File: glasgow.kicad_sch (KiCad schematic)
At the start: 90 parts, among them SW1 RST, U18 TPD3S014, U19 CY7C68013A-56LTX, U20 CAT24M01X, U21 BL24C256A-SFRC, U22 ICE40HX8K-BG121, U23 APX811-40UG-7, U24 TLV75533PDRVR, U25 TLV73312PQDRVR, Y2 24M

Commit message: more fixes, tweaks, pretty
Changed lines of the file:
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@@
 	(wire
 		(pts
-			(xy 217.17 106.68) (xy 217.17 109.22)
+			(xy 217.17 106.68) (xy 217.17 114.3)
 		)
 		(stroke
@@
 	)
 	(label "SWSH"
-		(at 217.17 109.22 270)
-		(effects
-			(font
+		(at 217.17 114.3 270)
+		(effects
+			(font

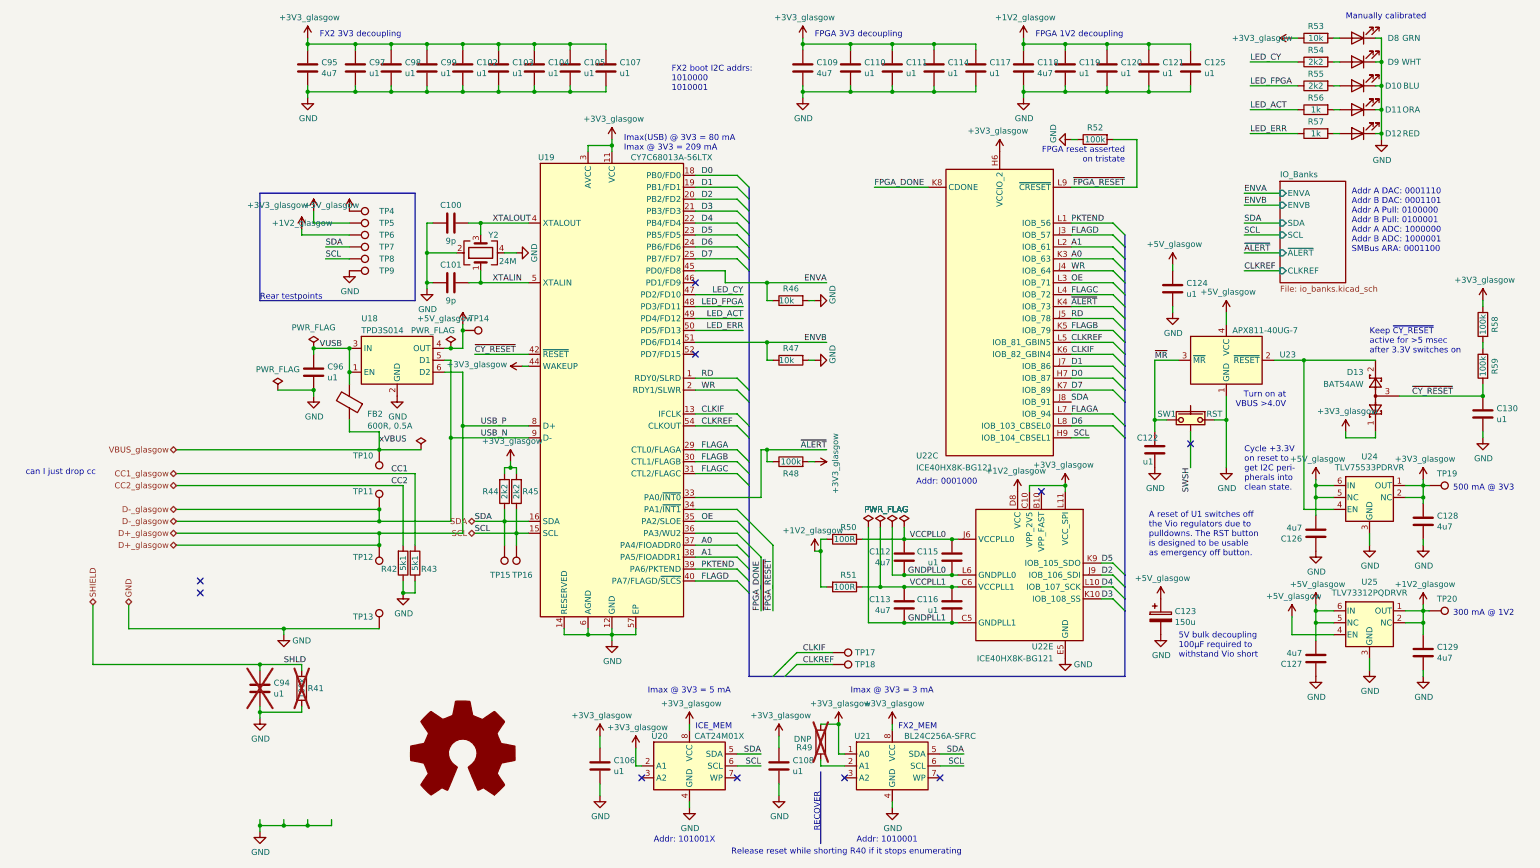
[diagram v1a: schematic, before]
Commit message: added USB-C
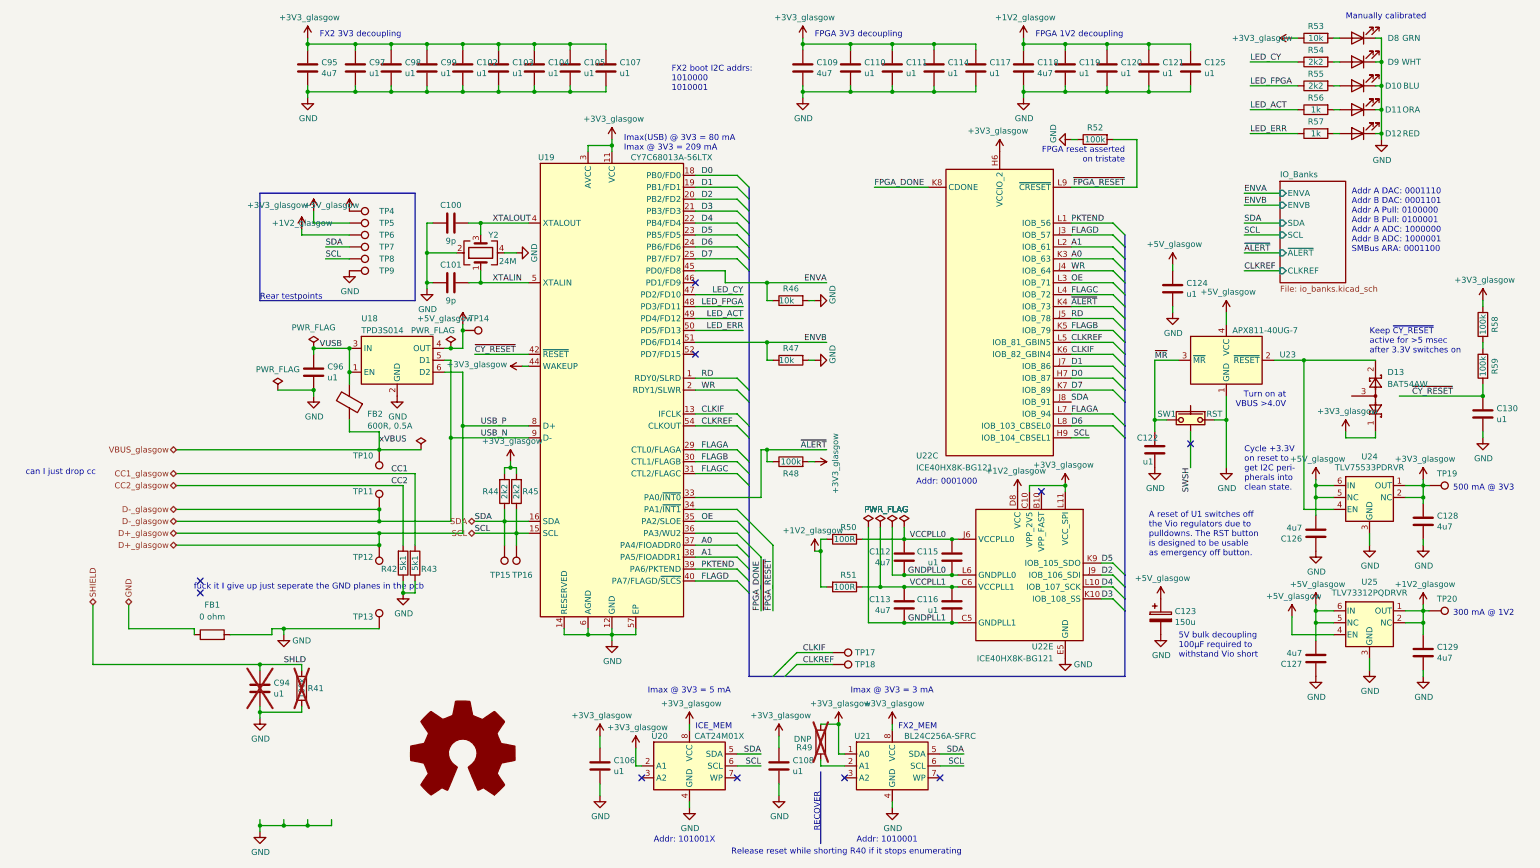
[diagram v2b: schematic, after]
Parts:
- added FB1: 0 ohm, A_HDJ_Library:Fuse_0805_2012Metric, symbol Device:R
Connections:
- net GND: now also FB1.1, FB1.2
- net ~{CY_RESET}: no longer D13.3
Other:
- note added: "fuck it I give up just seperate the GND planes in the pcb"
- moved on the sheet: D13
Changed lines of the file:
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@@
 		)
 	)
+	(text "fuck it I give up just seperate the GND planes in the pcb\n"
+		(exclude_from_sim no)
+		(at 29.464 139.7 0)
+		(effects
+			(font
+				(size 1.27 1.27)
+			)
+		)
+	)
 	(text "FX2_MEM"
 		(exclude_from_sim no)
@@
 	)
 	(junction
+		(at 24.13 148.59)
+		(diameter 0)
+		(color 0 0 0 0)
+	)
+	(junction
 		(at 156.21 129.54)
 		(diameter 0)
@@
 	)
 	(junction
-		(at 24.13 148.59)
-		(diameter 0)
-		(color 0 0 0 0)
-	)
-	(junction
 		(at 46.99 24.13)
 		(diameter 0)
@@
 	(wire
 		(pts
+			(xy 21.59 148.59) (xy 24.13 148.59)
+		)
+		(stroke
+			(width 0)
+			(type default)
+		)
+	)
+	(wire
+		(pts
 			(xy 92.71 34.29) (xy 85.09 34.29)
 		)
@@
 	(wire
 		(pts
+			(xy 24.13 148.59) (xy 44.45 148.59)
+		)
+		(stroke
+			(width 0)
+			(type default)
+		)
+	)
+	(wire
+		(pts
 			(xy 181.61 22.86) (xy 181.61 24.13)
 		)
@@
 		)
 	)
+	(wire
+		(pts
+			(xy 21.59 149.86) (xy 21.59 148.59)
+		)
+		(stroke
+			(width 0)
+			(type default)
+		)
+	)
 	(bus
 		(pts
@@
 	(wire
 		(pts
+			(xy 5.08 148.59) (xy 5.08 149.86)
+		)
+		(stroke
+			(width 0)
+			(type default)
+		)
+	)
+	(wire
+		(pts
 			(xy 59.69 107.95) (xy 76.2 107.95)
 		)
@@
 	(wire
 		(pts
-			(xy 24.13 148.59) (xy 44.45 148.59)
-		)
-		(stroke
-			(width 0)
-			(type default)
-		)
-	)
-	(wire
-		(pts
 			(xy 92.71 24.13) (xy 85.09 24.13)
 		)
@@
 	(wire
 		(pts
+			(xy 255.27 128.27) (xy 255.27 130.81)
+		)
+		(stroke
+			(width 0)
+			(type default)
+		)
+	)
+	(wire
+		(pts
 			(xy 39.37 34.29) (xy 46.99 34.29)
 		)
@@
 	(wire
 		(pts
+			(xy -8.89 148.59) (xy 5.08 148.59)
+		)
+		(stroke
+			(width 0)
+			(type default)
+		)
+	)
+	(wire
+		(pts
 			(xy 191.77 80.01) (xy 200.66 80.01)
 		)
@@
 	(wire
 		(pts
-			(xy -8.89 148.59) (xy 24.13 148.59)
-		)
-		(stroke
-			(width 0)
-			(type default)
-		)
-	)
-	(wire
-		(pts
-			(xy 255.27 128.27) (xy 255.27 130.81)
-		)
-		(stroke
-			(width 0)
-			(type default)
-		)
-	)
-	(wire
-		(pts
 			(xy 1.27 115.57) (xy 52.07 115.57)
 		)
@@
 	(wire
 		(pts
+			(xy 12.7 149.86) (xy 21.59 149.86)
+		)
+		(stroke
+			(width 0)
+			(type default)
+		)
+	)
+	(wire
+		(pts
 			(xy 111.76 52.07) (xy 120.65 52.07)
 		)
@@
 	(symbol
 		(lib_id "Diode:BAT54AW")
-		(at 256.54 99.06 90)
+		(at 256.54 99.06 270)
+		(mirror x)
 		(unit 1)
 		(body_style 1)
@@
 		(dnp no)
 		(property "Reference" "D13"
-			(at 254 93.98 90)
+			(at 259.08 93.98 90)
 			(show_name no)
 			(do_not_autoplace no)
@@
 		)
 		(property "Value" "BAT54AW"
-			(at 254 96.52 90)
+			(at 259.08 96.52 90)
 			(show_name no)
 			(do_not_autoplace no)
@@
 		)
 		(property "Footprint" "Glasgow:SOT-323_SC-70"
-			(at 253.365 97.155 0)
+			(at 259.715 97.155 0)
 			(hide yes)
 			(show_name no)
@@
 					(unit 1)
 				)
+			)
+		)
+	)
+	(symbol
+		(lib_id "Device:R")
+		(at 8.89 149.86 90)
+		(unit 1)
+		(body_style 1)
+		(exclude_from_sim no)
+		(in_bom yes)
+		(on_board yes)
+		(in_pos_files yes)
+		(dnp no)
+		(fields_autoplaced yes)
+		(property "Reference" "FB1"
+			(at 8.89 143.51 90)
+			(show_name no)
+			(do_not_autoplace no)
+			(effects
+				(font
+					(size 1.27 1.27)
+				)
+			)
+		)
+		(property "Value" "0 ohm"
+			(at 8.89 146.05 90)
+			(show_name no)
+			(do_not_autoplace no)
+			(effects
+				(font
+					(size 1.27 1.27)
+				)
+			)
+		)
+		(property "Footprint" "A_HDJ_Library:Fuse_0805_2012Metric"
+			(at 8.89 151.638 90)
+			(hide yes)
+			(show_name no)
+			(do_not_autoplace no)
+			(effects
+				(font
+					(size 1.27 1.27)
+				)
+			)
+		)
+		(property "Datasheet" ""
+			(at 8.89 149.86 0)
+			(hide yes)
+			(show_name no)
+			(do_not_autoplace no)
+			(effects
+				(font
+					(size 1.27 1.27)
+				)
+			)
+		)
+		(property "Description" "Resistor"
+			(at 8.89 149.86 0)
+			(hide yes)
+			(show_name no)
+			(do_not_autoplace no)
+			(effects
+				(font
+					(size 1.27 1.27)
+				)
+			)
+		)
+		(pin "1"
+		)
+		(pin "2"
+		)
+		(instances
+			(project "microcyber"
+				(path "/7ac319af-771c-4997-a005-b73a4a9b44ab/caa76144-87f3-4ce6-9e9c-dcd9e43abe5f"
+					(reference "FB1")
+					(unit 1)
+				)

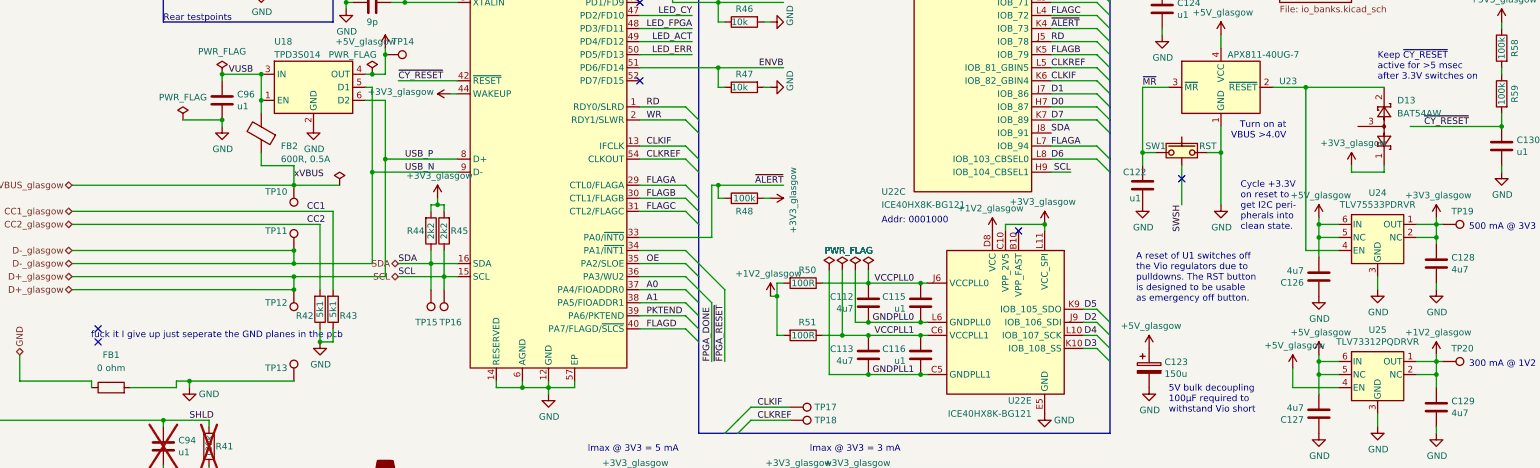
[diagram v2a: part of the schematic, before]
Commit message: added MPN to all parts by hand :'(
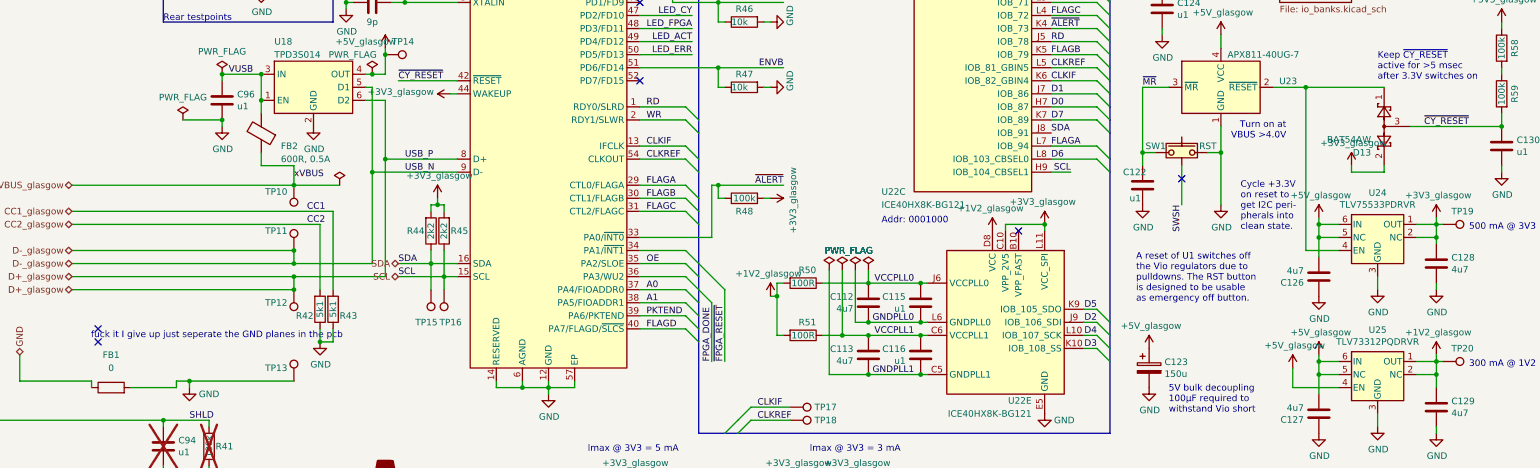
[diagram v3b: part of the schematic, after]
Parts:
- C102, C103, C104, C105, C106, C107, C108, C110, C111, C114, C115, C116, C117, C119, C120, C121, C122, C124, C125, C130, C96, C97, C98, C99: MPN TMK105BJ104KV-F -> C1005X7R1H104K050BE
- C109, C112, C113, C118, C126, C127, C128, C129: footprint Capacitor_SMD:C_0603_1608Metric -> A_DFRobot:C_0805_2012Metric; 1b2-bom-key cap-cer-0603-4u7 -> (none); MPN LMK107BJ475KAHT -> GRM21BR61H475KE51L; Mfg Taiyo Yuden -> (none)
- C95: footprint Capacitor_SMD:C_0603_1608Metric -> LED_SMD:LED_0805_2012Metric; 1b2-bom-key cap-cer-0603-4u7 -> (none); MPN LMK107BJ475KAHT -> GRM21BR61H475KE51L; Mfg Taiyo Yuden -> (none)
- FB1: value 0 ohm -> 0; MPN (none) -> MCS0402HZ0000ZE100
- R44, R45, R54, R55: MPN RC0402FR-132K2L -> RCS04022K20FKED
- R46, R47, R53: 1b2-bom-key res-0402-10k -> (none); MPN RC0402FR-1310KL -> RCS040210K0FKED; Mfg Yageo -> (none)
- R48, R52, R58, R59: 1b2-bom-key res-0402-100k -> (none); MPN RC0402FR-13100KL -> RCS0402100KFKED; Mfg Yageo -> (none)
- R56, R57: 1b2-bom-key res-0402-1k -> (none); MPN (none) -> RCS04021K00JNED
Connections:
- net +3V3_glasgow: now also D13.2; no longer D13.1
- net ~{CY_RESET}: now also D13.3
- net at U23.2 (~{RESET}), U24.4 (EN): now also D13.1; no longer D13.2
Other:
- moved on the sheet: D13
